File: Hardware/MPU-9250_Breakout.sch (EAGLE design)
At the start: 18 parts, among them U1 MPU-9250

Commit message: Fixed silk and info
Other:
- note added: "AD0/SDO defaults to 0V. This sets the I2C address to 0b1101000 and leaves the AD0/SDO PTH disconnected."
- note added: "VDD 2.4 to 3.6 V VDDIO 1.71 to VDD"
- note removed: "AD0/SDO defualts to 0V. This sets the I2C address to 0b1101000 and leaves the AD0/SDO PTH disconnected."
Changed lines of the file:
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@@
 <text x="165.608" y="11.43" size="2.54" layer="94" ratio="5">&gt;DESIGNER</text>
 <text x="236.982" y="7.112" size="2.794" layer="94" ratio="5">&gt;VERSION</text>
-<text x="127" y="45.72" size="1.778" layer="97" font="vector">AD0/SDO defualts to 0V.  This sets the
+<text x="127" y="45.72" size="1.778" layer="97" font="vector">AD0/SDO defaults to 0V.  This sets the
 I2C address to 0b1101000 and leaves
 the AD0/SDO PTH disconnected.</text>
@@
 of address</text>
 <text x="50.8" y="96.52" size="1.778" layer="97" font="vector" align="bottom-center">Set VDD and VDDIO equal by default</text>
+<text x="50.8" y="109.22" size="1.778" layer="97" font="vector" align="bottom-center">VDD 2.4 to 3.6 V
+VDDIO 1.71 to VDD</text>
 </plain>
 <instances>

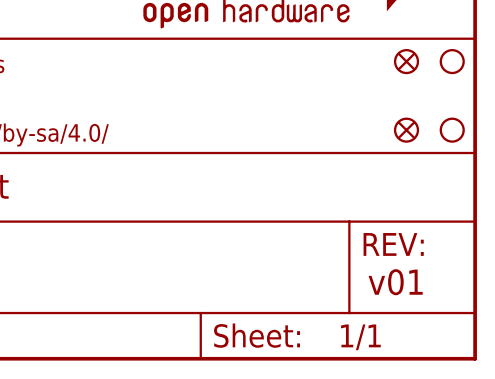
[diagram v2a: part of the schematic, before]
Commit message: Added stubs to NC pads on main IC and moved silk
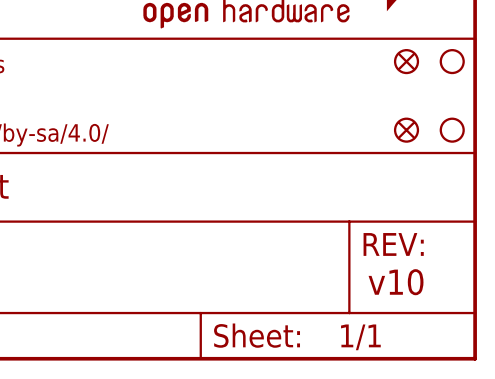
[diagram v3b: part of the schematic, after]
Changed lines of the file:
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@@
 <attributes>
 <attribute name="DESIGNER" value="Brent Wilkins"/>
-<attribute name="VERSION" value="v01"/>
+<attribute name="VERSION" value="v10"/>
 </attributes>
 <variantdefs>

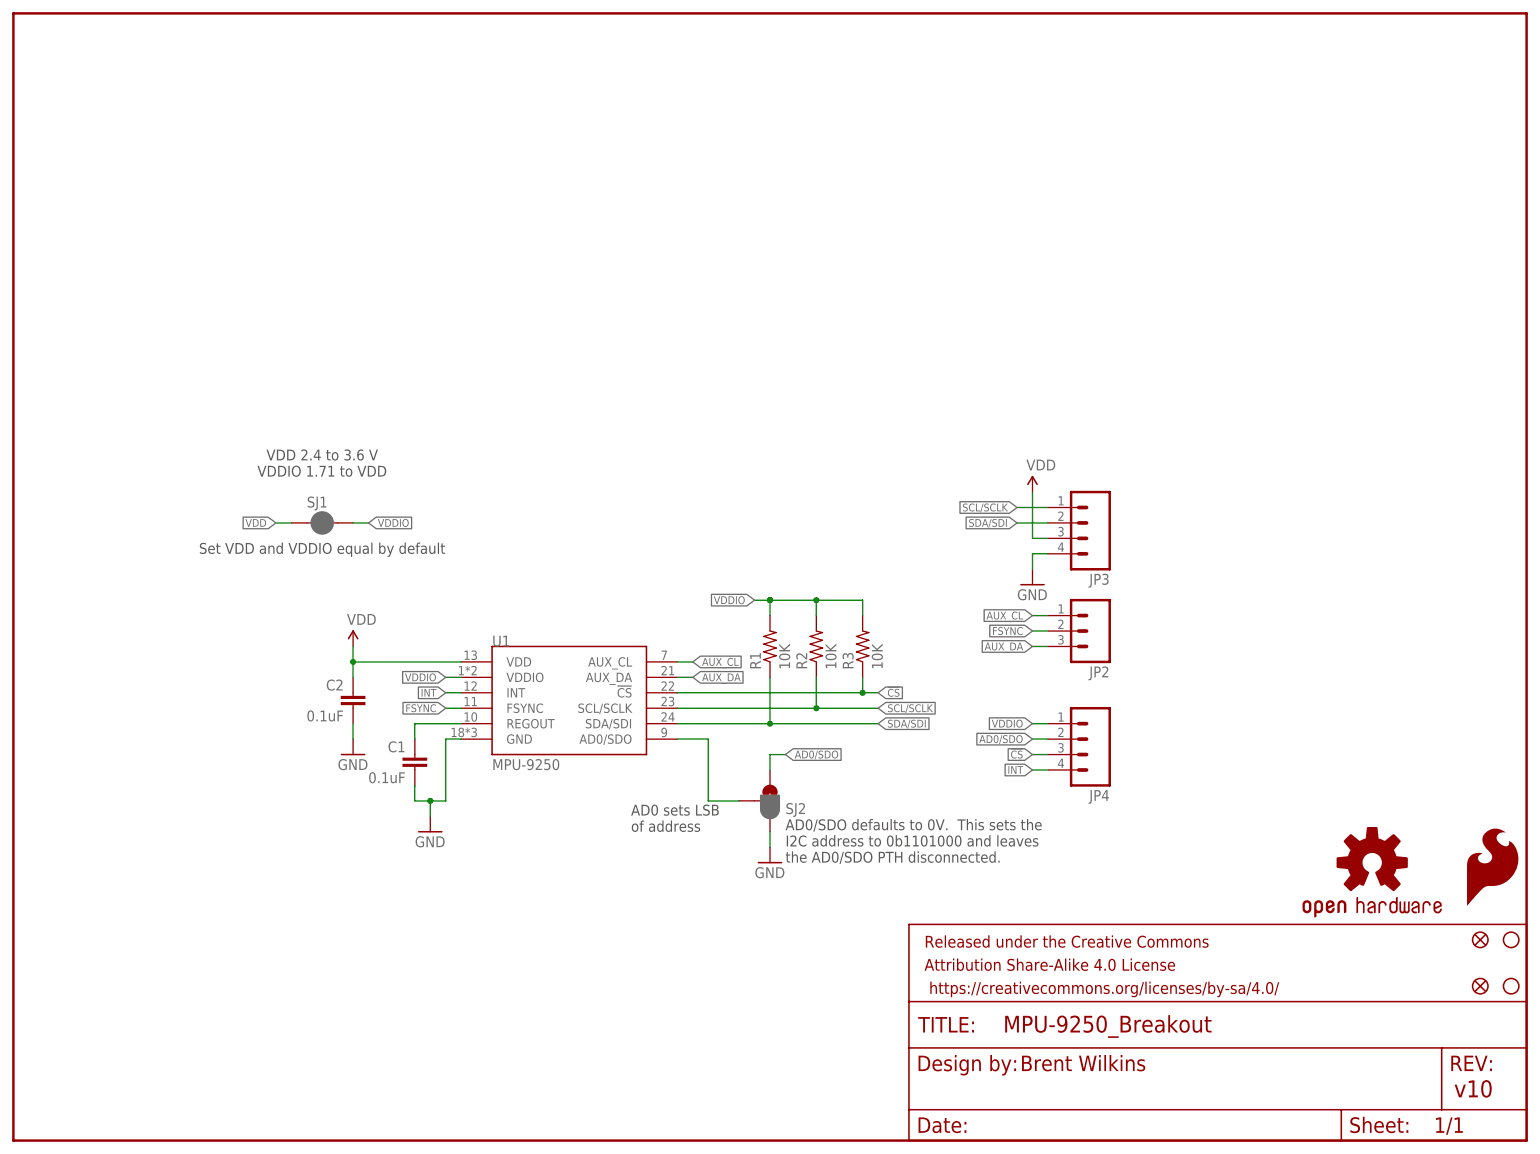
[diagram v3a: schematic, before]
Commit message: Removed bits of dimension on v-score
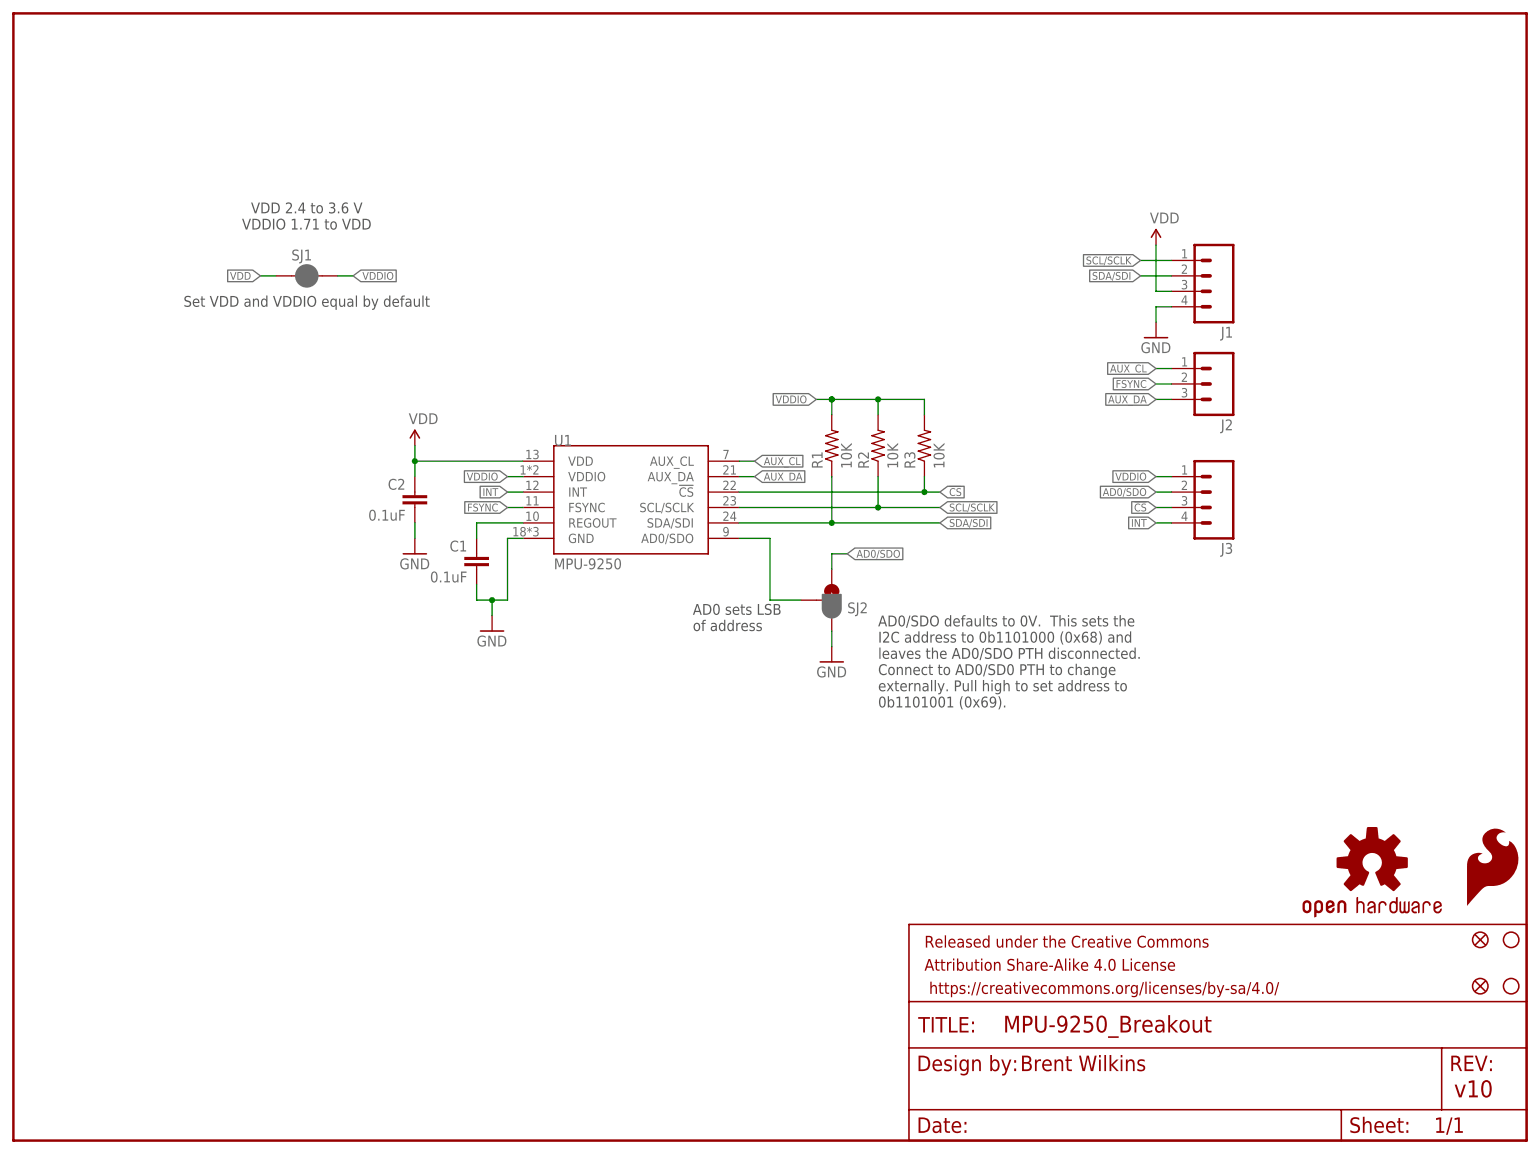
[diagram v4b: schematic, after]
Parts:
- removed JP2: (no value), SparkFun-Connectors:M03PTH
- removed JP3, JP4: (no value), SparkFun-Connectors:M04PTH
- added J1, J3: (no value), SparkFun-Connectors:M04PTH
- added J2: (no value), SparkFun-Connectors:M03PTH
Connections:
- net !CS: now also J3.3; no longer JP4.3
- net AD0/SDO: now also J3.2; no longer JP4.2
- net AUX_CL: now also J2.1; no longer JP2.1
- net AUX_DA: now also J2.3; no longer JP2.3
- net FSYNC: now also J2.2; no longer JP2.2
- net GND: now also J1.4; no longer JP3.4
- net INT: now also J3.4; no longer JP4.4
- net SCL/SCLK: now also J1.1; no longer JP3.1
- net SDA/SDI: now also J1.2; no longer JP3.2
- net VDD: now also J1.3; no longer JP3.3
- net VDDIO: now also J3.1; no longer JP4.1
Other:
- note added: "AD0/SDO defaults to 0V. This sets the I2C address to 0b1101000 (0x68) and leaves the AD0/SDO PTH disconnected. Connect to AD0/SD0 PTH to change externally. Pull high to set address to 0b1101001 (0x69)."
- note removed: "AD0/SDO defaults to 0V. This sets the I2C address to 0b1101000 and leaves the AD0/SDO PTH disconnected."
- moved on the sheet: C1, C2, R1, R2, R3, SJ1, SJ2, U1
